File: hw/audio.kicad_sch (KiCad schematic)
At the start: 40 parts, among them J10 SJ-43516-SMT-TR, J9 SPKR_L, J9 SPKR_R, Q1 2N3904, U3 TLV70033_SOT23-5, U4 NC7WZ16P6X, U4 TPA2012D2RTJT

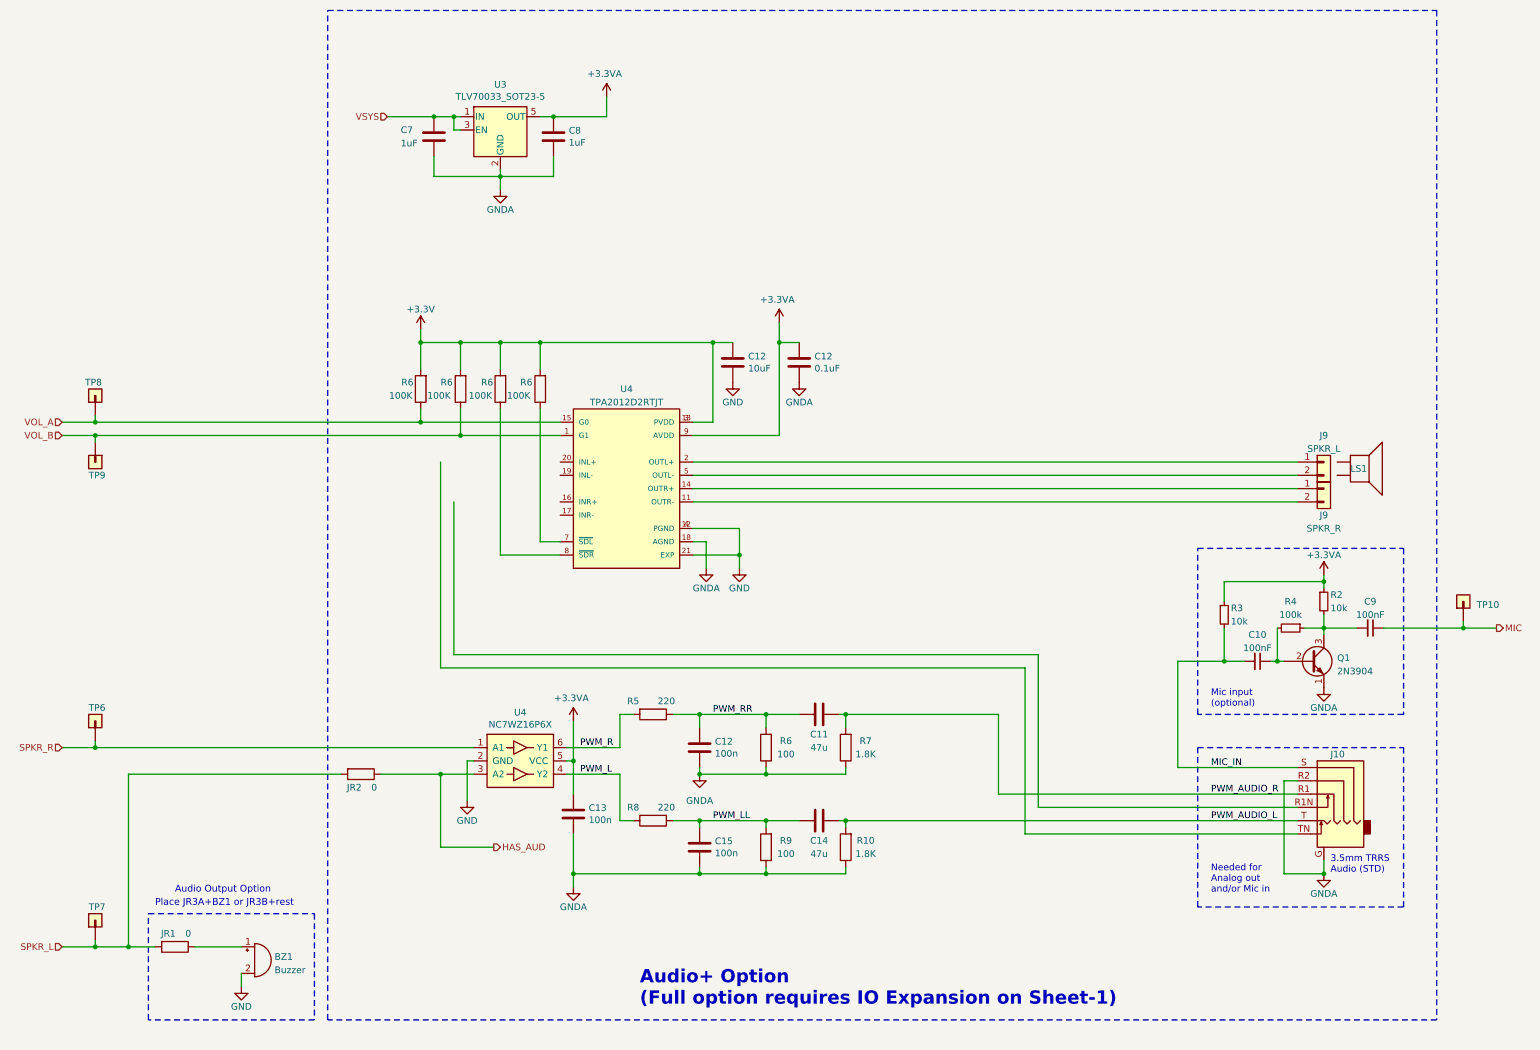
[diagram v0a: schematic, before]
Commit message: Schematic prior to pulling KOB interface to separate board.
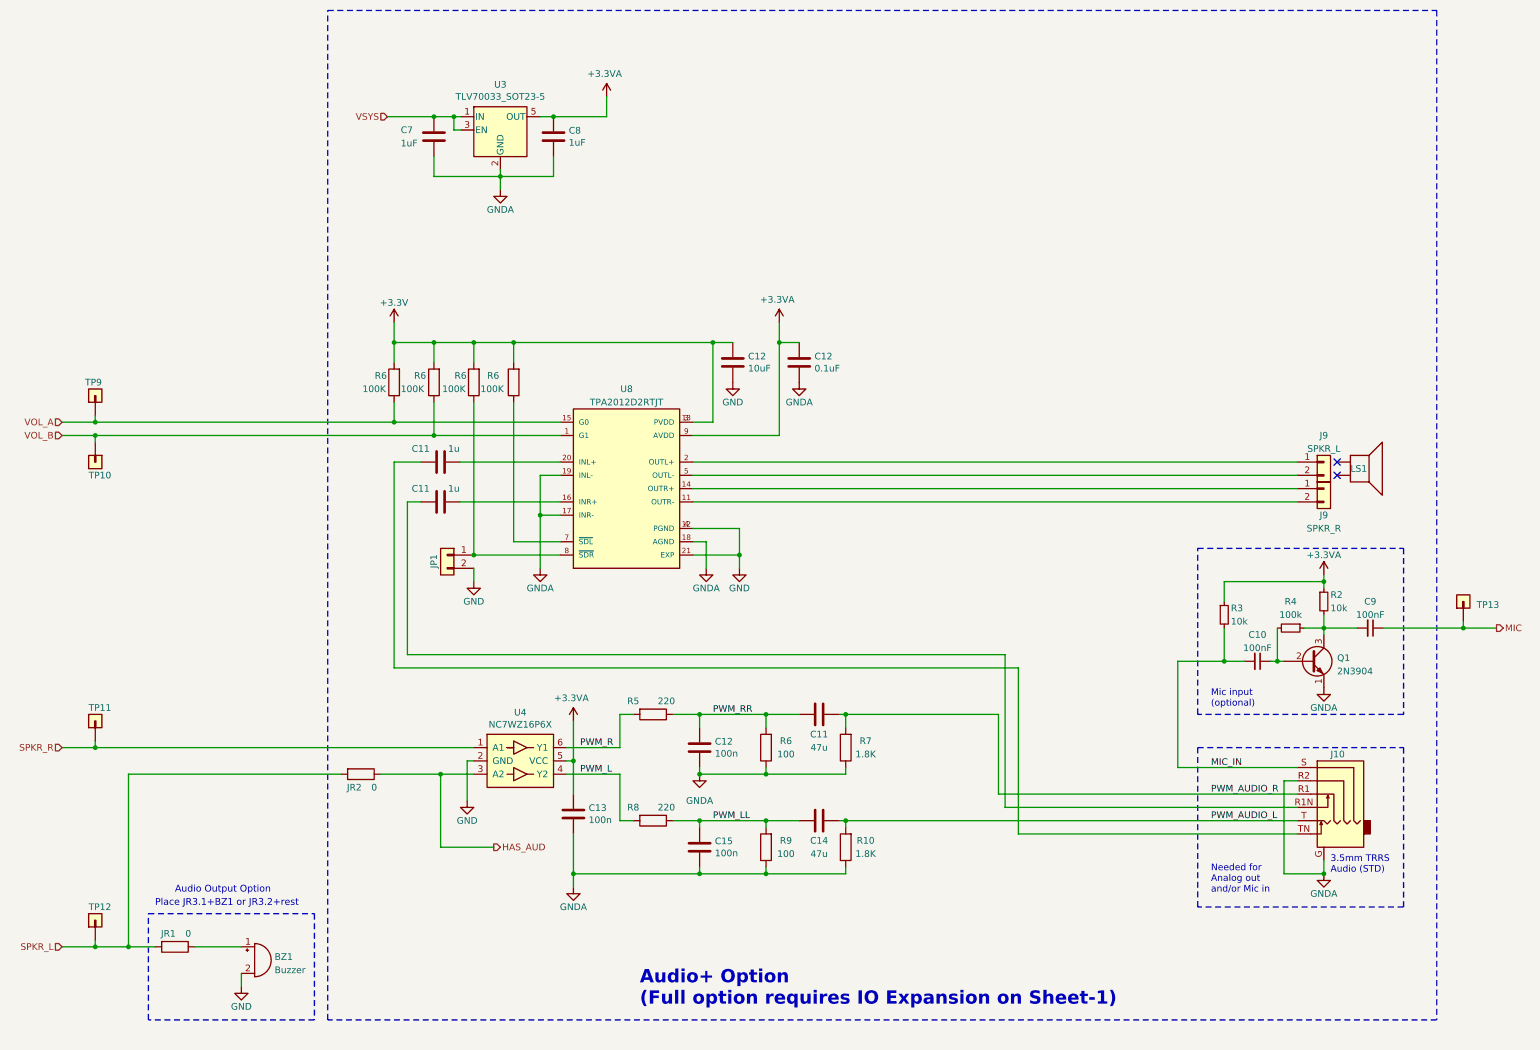
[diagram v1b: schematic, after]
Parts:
- added C11 (x2): 1u, Capacitor_SMD:C_0805_2012Metric, symbol Device:C
- added JP1: Conn_01x02, symbol Connector_Generic:Conn_01x02
- renumbered TP9 to TP10, TP6 to TP11, TP7 to TP12, TP10 to TP13, TP8 to TP9, U4 to U8
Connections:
- net GND: now also JP1.2 (Pin_2)
- net GNDA: now also U8.17 (INR-), U8.19 (INL-)
- net at J10.R1N: now also C11.2
- net at J10.TN: now also C11.2
- net at R6.1, U8.8 (~{SDR}): now also JP1.1 (Pin_1)
- net at U8.16 (INR+): now also C11.1
- net at U8.20 (INL+): now also C11.1
- no-connect marks 0 -> 2
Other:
- note added: "Place JR3.1+BZ1 or JR3.2+rest"
- note removed: "Place JR3A+BZ1 or JR3B+rest"
- moved on the sheet: R6

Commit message: Audio on main page. KeySounder Intf on separate board. Switch matrix via Resistors.
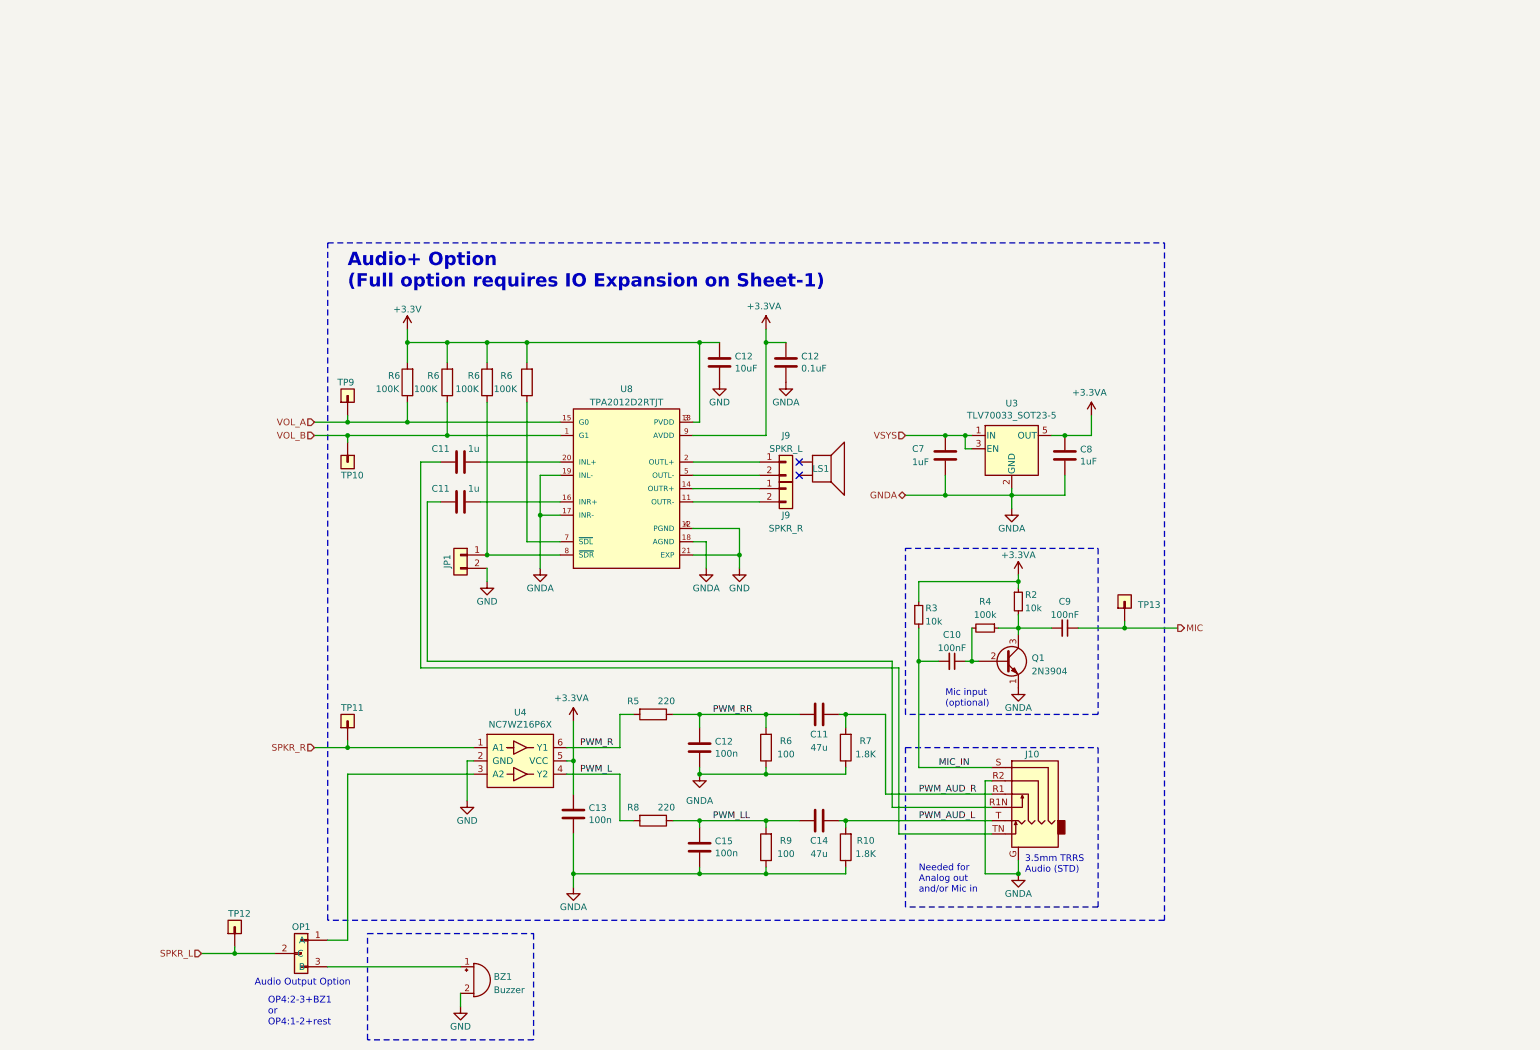
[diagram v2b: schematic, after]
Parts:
- removed JR1, JR2: 0, Resistor_SMD:R_0000_1005Metric, symbol Device:R
- added OP1: OP_A-B, Connector_PinHeader_1.00mm:PinHeader_1x03_P1.00mm_Vertical, symbol MuKOB:Option_A-B
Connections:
- net SPKR_L: now also OP1.2 (C)
- net at BZ1.1 (-): now also OP1.3 (B)
- net HAS_AUD: no longer names the net of U4.3 (A2)
- net HAS_AUD: now also OP1.1 (A)
- net PWM_AUDIO_L renamed PWM_AUD_L
- net PWM_AUDIO_R renamed PWM_AUD_R
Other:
- note added: "OP4:2-3+BZ1 or OP4:1-2+rest"
- note removed: "Place JR3.1+BZ1 or JR3.2+rest"
- company: AESilky -> Silky-Design (AESilky)
- moved on the sheet: BZ1, C10, C11, C12, C7, C8, C9, J10, J9, JP1, LS1, Q1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
